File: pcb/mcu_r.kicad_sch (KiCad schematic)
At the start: 30 parts, among them J4 USB_C_Receptacle_USB2.0_16P, SW3 RESET, SW4 BOOTSEL, U4 AMS1117-3.3, U5 RP2040, U6 W25Q128JVS, Y2 ABM8-272-T3

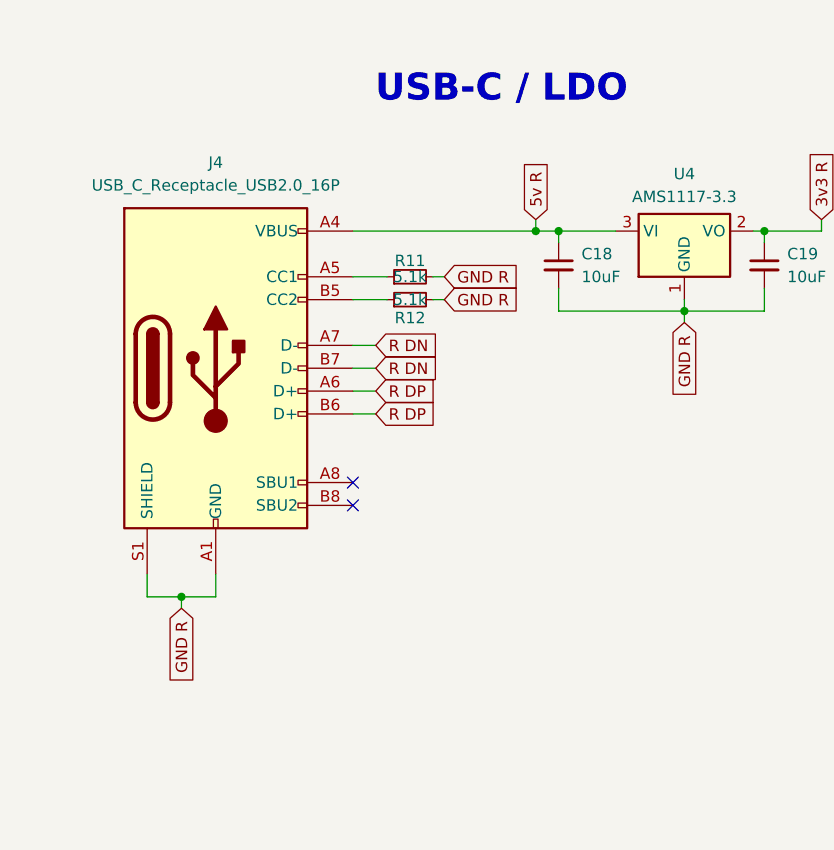
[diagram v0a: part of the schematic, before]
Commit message: Initial PCB v1.1.0 updates, including 4-layer restructure
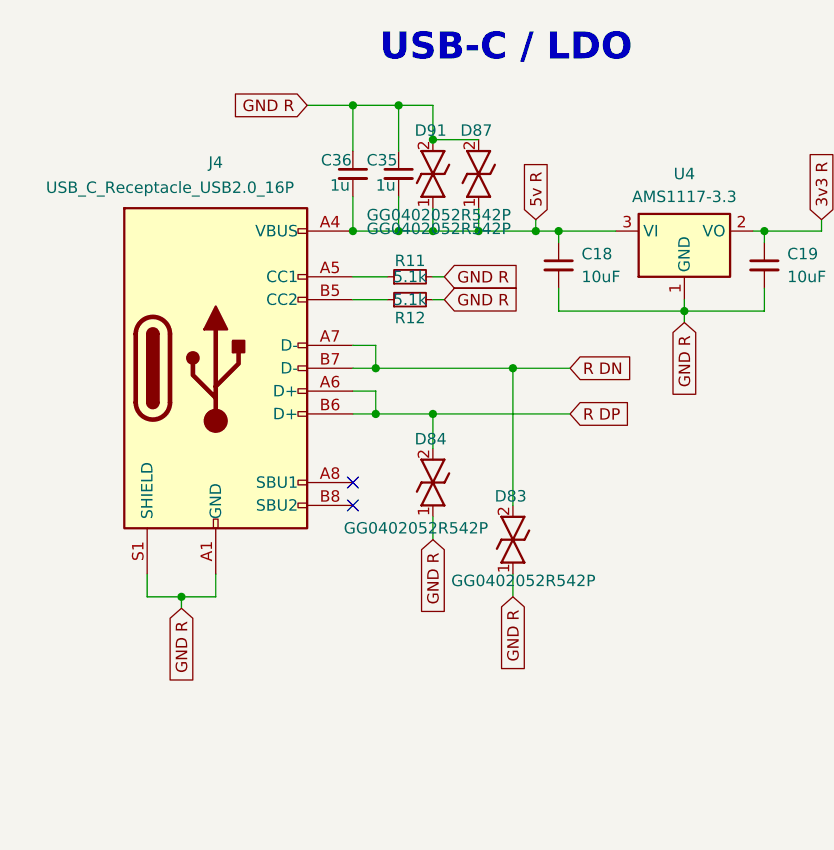
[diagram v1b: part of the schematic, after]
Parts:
- added C35, C36: 1u, Capacitor_SMD:C_0603_1608Metric, symbol Device:C_Small
- added D83, D84, D87, D91: GG0402052R542P, GG0402052R542P:DIONC1006X55N, symbol GG0402052R542P:GG0402052R542P
- SW3, SW4: footprint Button_Switch_SMD:SW_SPST_EVQP0 -> EVQ-P9P02W:EVQ-P9P02W
- U6: footprint Package_SO:SOIC-8_5.23x5.23mm_P1.27mm -> W25Q128JVSIQ:SOIC127P790X216-8N
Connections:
- net 5v R: now also C35.2, C36.2, D87.1, D91.1
- net GND R: now also C35.1, C36.1, D83.1, D84.1, D87.2, D91.2
- net R DN: now also D83.2
- net R DP: now also D84.2

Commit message: Include components as a path in the repository
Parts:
- SW3, SW4: footprint EVQ-P9P02W:EVQ-P9P02W -> EVQ-P9P02W:EVQP2202M
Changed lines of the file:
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@@
 			)
 		)
-		(property "Footprint" "EVQ-P9P02W:EVQ-P9P02W"
+		(property "Footprint" "EVQ-P9P02W:EVQP2202M"
 			(at 157.48 157.48 0)
 			(hide yes)
@@
 			)
 		)
-		(property "Footprint" "EVQ-P9P02W:EVQ-P9P02W"
+		(property "Footprint" "EVQ-P9P02W:EVQP2202M"
 			(at 201.93 60.96 0)
 			(hide yes)
